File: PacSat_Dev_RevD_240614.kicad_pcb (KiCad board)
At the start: 6 copper layers, 92 x 92 mm, 344 parts, among them J2 CONN_02X05, J801 Conn_02x05_Odd_Even, P101 U_FL, P601 U_FL, P651 Conn_04x26_Pin, P702 U_FL, P703 U_FL, Q601 SAV-331+, Q701 ATF05MS004NT1, T601 ADT4-1WT+, U156 AX5043, U2 TMS570LS0914PGE, U201 RFShield_OnePiece, U205 AX5043, U206 TLP3905, U26 DS28E83Q+T, U28 MAX31331TETB+, U29 MAX31725MTA+, U30 MAX31725MTA+, U301 RFShield_OnePiece, U305 AX5043, U401 RFShield_OnePiece, U405 AX5043, U501 RFShield_OnePiece, U505 AX5043, U602 LT6657AHMS8-2.5, U604 RBP-140+, U652 CDCLVC1106, U701 RFShield_OnePiece, U705 SXBP-425+, U76 MR25H40CDE, U77 MR25H40CDE, U78 MR25H40CDE, U79 MR25H40CDE, U86 TPS7A7001DDA, U87 MAX1556AEBT+, U88 MAX1556A, U89 TPS22917DBV, U90 STWD100NYWY3F, U91 MAX4995ALAUT, U92 MAX4995ALAUT, U93 MAX4995ALAUT, U94 MAX4995ALAUT, U95 STWD100NYWY3F, Y26 AB26T-32.768KHZ-6B, Y601 588S160X2CAT, Y602 ECS-TXO-2016-33-160-TR

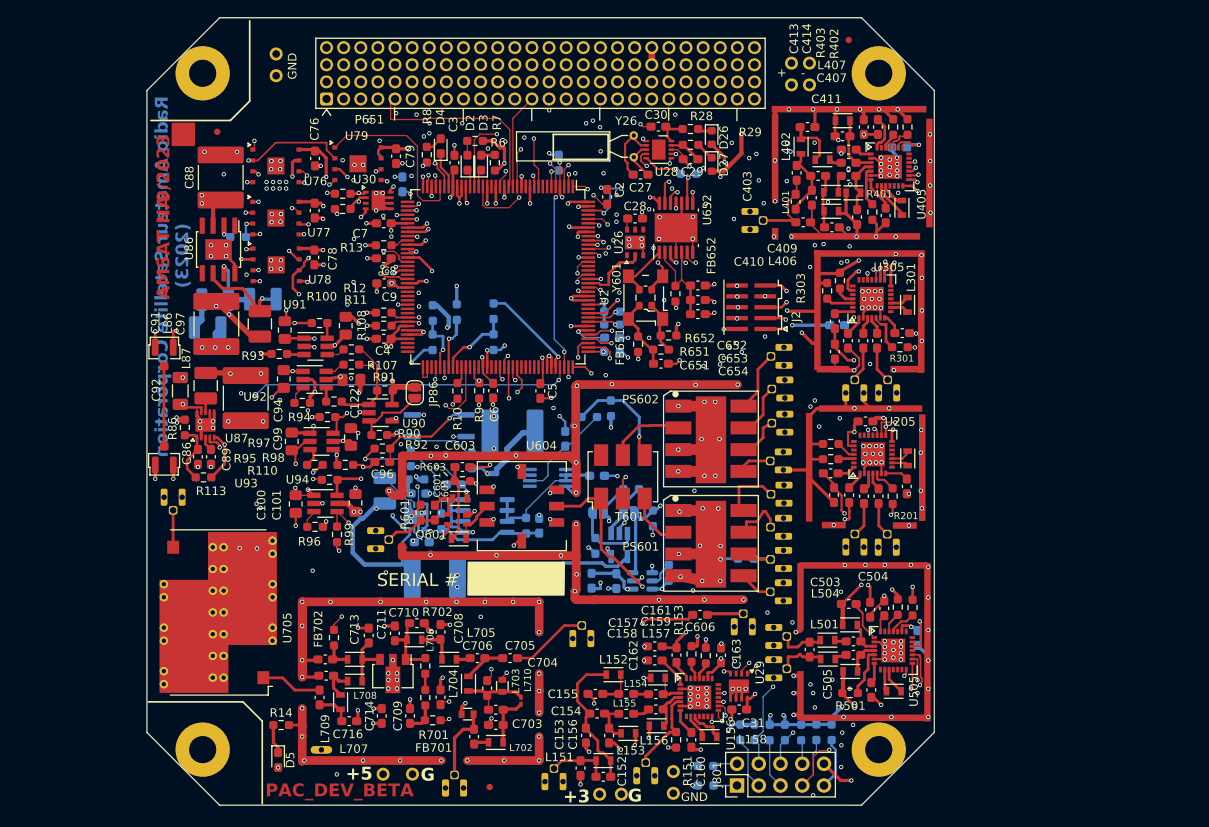
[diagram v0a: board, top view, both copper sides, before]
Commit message: Lots of cleanups to fix numerous issues
Signed-off-by: Corey Minyard <corey@minyard.net>
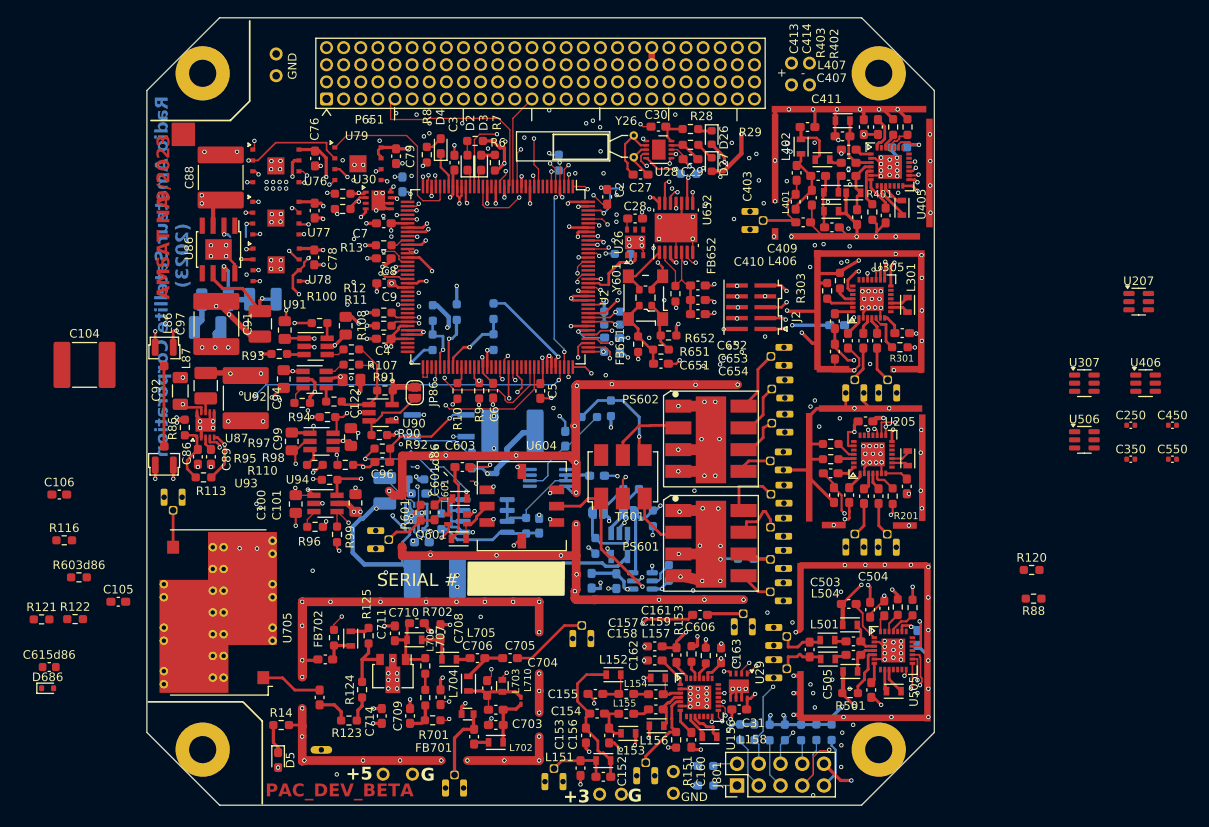
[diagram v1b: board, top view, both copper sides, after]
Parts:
- removed C601: 2.2 nF, Capacitor_SMD:C_0603_1608Metric_Pad1.08x0.95mm_HandSolder
- removed C602: 0.1 u, Capacitor_SMD:C_0603_1608Metric_Pad1.08x0.95mm_HandSolder
- removed C713, C715, C716: 2200p, Capacitor_SMD:C_0603_1608Metric_Pad1.08x0.95mm_HandSolder
- removed L708: 2n55, PacSatDev_misc:L_Murata_LQH2MCNxxxx02_2.0x1.6mm
- removed L709: 8n1, PacSatDev_misc:L_Murata_LQH2MCNxxxx02_2.0x1.6mm
- removed R602: 10K, Resistor_SMD:R_0603_1608Metric_Pad0.98x0.95mm_HandSolder
- removed R603: 1K, Resistor_SMD:R_0603_1608Metric_Pad0.98x0.95mm_HandSolder
- removed REF** (x3): Fiducial_0.75mm_Mask1.5mm, Fiducial:Fiducial_0.75mm_Mask1.5mm
- added C104: 10u 10v, Capacitor_SMD:C_2220_5750Metric_Pad1.97x5.40mm_HandSolder, F.Cu at (142.7, 98.6)
- added C105: 0.1 u, Capacitor_SMD:C_0603_1608Metric_Pad1.08x0.95mm_HandSolder, F.Cu at (146.7, 126.2)
- added C106: 0.1 u, Capacitor_SMD:C_0603_1608Metric_Pad1.08x0.95mm_HandSolder, F.Cu at (139.8, 113.7)
- added C250: .1u, Capacitor_SMD:C_0402_1005Metric, F.Cu at (264.9, 105.6)
- added C350: .1u, Capacitor_SMD:C_0402_1005Metric, F.Cu at (264.9, 109.6)
- added C450: .1u, Capacitor_SMD:C_0402_1005Metric, F.Cu at (269.8, 105.6)
- added C550: .1u, Capacitor_SMD:C_0402_1005Metric, F.Cu at (269.8, 109.6)
- added C601d86: 6p, Capacitor_SMD:C_0603_1608Metric_Pad1.08x0.95mm_HandSolder, F.Cu at (183.6, 115.8)
- added C615d86: 10u, Capacitor_SMD:C_0603_1608Metric, F.Cu at (138.6, 133.9)
- added D686: BZX58550-C1V8-QX, Diode_SMD:D_SOD-523, F.Cu at (138.4, 136.3)
- added R116: 440K, Resistor_SMD:R_0603_1608Metric_Pad0.98x0.95mm_HandSolder, F.Cu at (140.3, 119.0)
- added R120: 10 1/2 W, Resistor_SMD:R_0603_1608Metric_Pad0.98x0.95mm_HandSolder, F.Cu at (253.4, 122.5)
- added R121: 580K, Resistor_SMD:R_0603_1608Metric_Pad0.98x0.95mm_HandSolder, F.Cu at (137.7, 128.3)
- added R122: 420K, Resistor_SMD:R_0603_1608Metric_Pad0.98x0.95mm_HandSolder, F.Cu at (141.6, 128.3)
- added R123: 0, Resistor_SMD:R_0603_1608Metric_Pad0.98x0.95mm_HandSolder, F.Cu at (173.6, 140.1)
- added R124: 0, Resistor_SMD:R_0603_1608Metric_Pad0.98x0.95mm_HandSolder, F.Cu at (175.1, 136.5)
- added R125: 50, Resistor_SMD:R_0603_1608Metric_Pad0.98x0.95mm_HandSolder, F.Cu at (175.9, 130.2)
- added R126: 20K, Resistor_SMD:R_0603_1608Metric_Pad0.98x0.95mm_HandSolder, B.Cu at (205.6, 85.6)
- added R603d86: 27 1/2 Watt, Resistor_SMD:R_0603_1608Metric_Pad0.98x0.95mm_HandSolder, F.Cu at (142.1, 123.4)
- added U207: TPS22929D, Package_TO_SOT_SMD:SOT-23-6, F.Cu at (265.9, 91.2)
- added U307: TPS22929D, Package_TO_SOT_SMD:SOT-23-6, F.Cu at (259.5, 100.7)
- added U406: TPS22929D, Package_TO_SOT_SMD:SOT-23-6, F.Cu at (266.7, 100.7)
- added U506: TPS22929D, Package_TO_SOT_SMD:SOT-23-6, F.Cu at (259.5, 107.3)
- C606: value 1u -> 1n
- C88: value 10u -> 16V; footprint Capacitor_SMD:C_2220_5650Metric_Pad1.97x5.40mm_HandSolder -> Capacitor_SMD:C_2220_5750Metric_Pad1.97x5.40mm_HandSolder
- C91: value 22u -> 22u 10V; footprint Capacitor_SMD:C_2220_5650Metric_Pad1.97x5.40mm_HandSolder -> Capacitor_SMD:C_2220_5750Metric_Pad1.97x5.40mm_HandSolder
- C93, C94, C95: footprint Capacitor_SMD:C_2220_5650Metric_Pad1.97x5.40mm_HandSolder -> Capacitor_SMD:C_2220_5750Metric_Pad1.97x5.40mm_HandSolder
- D26, D27: value RB521CS30L,315 -> RB521CS30L,315
- R601: value 5 Meg -> 500K
- R606: value 5K -> 47K
- R701: value 22 -> 50
- R702: value 22 -> 0
- R88: value 4.7k -> 20; moved to F.Cu
- R89: value 10 -> 2 1/4 W
- R98, R99: value 4.7k -> 10K
- moved R88 102.1 mm to (253.6, 125.9)
- moved L707 2.48 mm to (173.8, 130.5), turned to -90 degrees
- turned R99 to 90 degrees
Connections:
- net -2V BIAS renamed -7V BIAS
- net Net-(J2-P10) renamed Optional Reset Push Button
- C207 pad 1: AX5043_3V3 -> Net-(U205-VDD_IO)
- C307 pad 1: AX5043_3V3 -> Net-(U305-VDD_IO)
- C415 pad 1: AX5043_3V3 -> Net-(U405-VDD_IO)
- C508 pad 1: AX5043_3V3 -> Net-(U505-VDD_IO)
- C605 pad 1: Net-(U602-Vin) -> +3.3V
- C91 pad 1: REG_5.0V -> Net-(U86-OUT)
- FB701 pad 1: +5V -> Net-(FB701-Pad1)
- L707 pad 1: Net-(Q701-D) -> Net-(L707-Pad1)
- Q602 pad 1: Net-(U602-Vin) -> +3.3V
- Q602 pad 2: Net-(U602-Vin) -> +3.3V
- Q602 pad 3: Net-(U602-Vin) -> +3.3V
- R11 pad 1: GND -> +3.3V
- R12 pad 1: +3.3V -> GND
- R604 pad 2: Net-(T601-SC) -> unconnected-(R604-Pad2)
- R605 pad 1: Net-(T601-SC) -> unconnected-(R605-Pad1)
- R607 pad 2: Net-(U602-Vin) -> +3.3V
- R88 pad 1: +3.3V -> Net-(R88-Pad1)
- R88 pad 2: REG_5V_EN -> Net-(U88-INP)
- R98 pad 1: PWR_SW_AX5043 -> AX5043 PWR CTL
- R99 pad 1: PWR_SW_SSPA -> +3.3V
- R99 pad 2: GND -> PA PWR CTL
- T601 pad 4: Net-(T601-SC) -> GND
- U2 pad 31: REG_5V_EN -> unconnected-(U2-N2HET1_5-Pad31)
- U2 pad 78: PWR_SW_SSPA -> unconnected-(U2-AD1IN_5-Pad78)
- U2 pad 83: PWR_SW_AX5043 -> unconnected-(U2-AD1IN_8-Pad83)
- U2 pad 98: unconnected-(U2-MIBSPI5SOMI_0-Pad98) -> PA PWR CTL
- U2 pad 99: unconnected-(U2-MIBSPI5SIMO_0-Pad99) -> AX5043 PWR CTL
- U205 pad 23: AX5043_3V3 -> Net-(U205-VDD_IO)
- U206 pad 2: Net-(U88-INP) -> Net-(R88-Pad1)
- U29 pad 5: GND -> AX5043_3V3
- U29 pad 7: GND -> I2C_SCL
- U30 pad 5: GND -> +3.3V
- U30 pad 7: GND -> I2C_SDA
- U305 pad 23: AX5043_3V3 -> Net-(U305-VDD_IO)
- U405 pad 23: AX5043_3V3 -> Net-(U405-VDD_IO)
- U505 pad 23: AX5043_3V3 -> Net-(U505-VDD_IO)
- U602 pad 2: Net-(U602-Vin) -> +3.3V
- U602 pad 3: Net-(U602-Vin) -> +3.3V
- U86 pad 2: REG_5V_EN -> VSYS
- U93 pad 4: PWR_SW_AX5043 -> AX5043 PWR CTL
- U94 pad 4: PWR_SW_SSPA -> PA PWR CTL
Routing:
- net PA PWR CTL: track 0.00 -> 46.5 mm, vias 0 -> 3
- net REG_5V_EN: track 40.6 -> 0.00 mm, vias 3 -> 0
- net AX5043 PWR CTL: track 0.00 -> 33.4 mm, vias 0 -> 3
- net PWR_SW_SSPA: track 33.3 -> 0.00 mm, vias 3 -> 0
- net AX5043_MOSI: track 181.0 -> 212.7 mm
- net PWR_SW_AX5043: track 26.0 -> 0.00 mm, vias 3 -> 0
- net +3.3V: track 162.8 -> 180.3 mm, vias 57 -> 58
- net Net-(U602-Vin): track 15.4 -> 0.00 mm
- net Net-(T601-SC): track 13.1 -> 0.00 mm, vias 1 -> 0
- net GND: track 708.8 -> 714.3 mm, vias 378 -> 375
- net Net-(C715-Pad1): track 4.48 -> 0.00 mm
- net Net-(R123-Pad2): track 0.00 -> 3.03 mm
- net Net-(L707-Pad1): track 0.00 -> 2.25 mm
- net VSYS: track 47.0 -> 48.9 mm, vias 4 -> 5
- net Net-(C717-Pad1): track 5.68 -> 4.40 mm
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
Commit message: Add notes file with todos and history, more cleanups
Signed-off-by: Corey Minyard <corey@minyard.net>
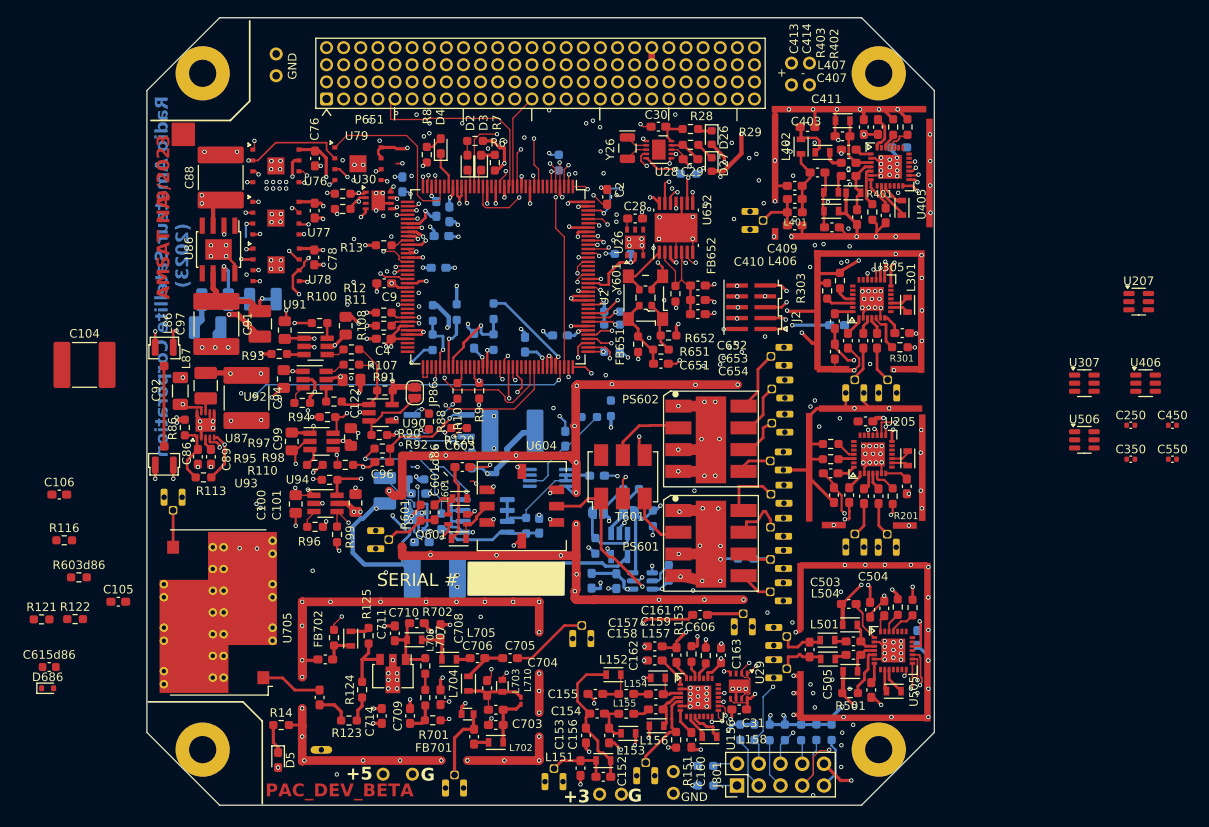
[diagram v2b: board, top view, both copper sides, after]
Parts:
- removed C27: 6p, Capacitor_SMD:C_0603_1608Metric_Pad1.08x0.95mm_HandSolder
- C3, C5, C6, C7, C79, C8: moved to B.Cu
- Y26: value AB26T-32.768KHZ-6B -> 32.768kHz; footprint Crystal:Crystal_AT310_D3.0mm_L10.0mm_Horizontal -> Crystal:Crystal_SMD_EuroQuartz_EQ161-2Pin_3.2x1.5mm
- moved R88 73.6 mm to (183.0, 105.2), turned to -90 degrees
- moved R120 68.9 mm to (186.5, 105.9), turned to 180 degrees
- moved C79 7.75 mm to (183.8, 80.3), turned to 90 degrees
- moved C7 6.90 mm to (184.4, 83.5), turned to 0 degrees
- moved C8 6.49 mm to (184.1, 87.2), turned to 0 degrees
- moved C6 6.24 mm to (188.2, 95.7), turned to 90 degrees
- moved C10 6.09 mm to (198.3, 95.1), turned to 180 degrees
- moved C3 6.07 mm to (185.3, 81.0), turned to -90 degrees
- moved C5 5.69 mm to (194.2, 96.2), turned to 90 degrees
- moved C402 3.06 mm to (225.7, 79.2), turned to 180 degrees
- moved C403 2.43 mm to (225.7, 77.6), turned to 180 degrees
- moved Y26 1.65 mm to (206.1, 73.2)
- moved L401 1.23 mm to (225.7, 80.7), turned to 0 degrees
- moved C401 1.05 mm to (225.7, 82.3)
- moved L404 0.86 mm to (228.9, 73.7)
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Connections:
- R120 pad 1: Net-(U88-INP) -> GND
- R88 pad 2: Net-(U88-INP) -> GND
- U88 pad 9: Net-(U88-INP) -> REG_5.0V
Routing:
- net AX5043_3V3: track 220.4 -> 173.1 mm, vias 11 -> 5
- net AX5043_MOSI: track 212.7 -> 184.1 mm
- net Net-(U88-INP): track 12.4 -> 0.00 mm, vias 2 -> 0
- net GND: track 714.3 -> 702.1 mm, vias 375 -> 376
- net Net-(U28-X2): track 7.50 -> 2.58 mm
- net I2C_SCL: track 124.6 -> 128.9 mm
- net +3.3V: track 180.3 -> 183.8 mm, vias 58 -> 60
- net Net-(P401-In): track 9.62 -> 6.31 mm
- net +1V2: track 147.8 -> 144.8 mm
- net Net-(U86-OUT): track 11.2 -> 14.1 mm
- net Net-(R88-Pad1): track 0.00 -> 2.87 mm, vias 0 -> 1
- net Net-(R120-Pad2): track 7.74 -> 10.4 mm, vias 0 -> 1
- net REG_5.0V: track 110.5 -> 112.4 mm
- net Net-(U28-X1): track 4.54 -> 2.64 mm
- net REG_3V3: track 108.4 -> 110.0 mm
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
